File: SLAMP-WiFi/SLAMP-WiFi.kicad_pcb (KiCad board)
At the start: 2 copper layers, 61.6 x 47.2 mm, 50 parts, among them P1 POWER_IN 5V, P10 FACE5, P2 USB_BUS, P3 VUSB, P4 EXTRA, P5 ADC, P6 FACE1, P7 FACE2, P8 FACE3, P9 FACE4, Q1 S8050, Q2 S8050, SW1 KEY_RST, SW2 KEY_FLASH, U1 MIC5219-3.3BM5, U2 CH340G, U3 ESP-12F, Y1 12 MHz

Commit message: Serigrafia terminada
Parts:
- removed G***: LOGO, mod:wifilogo
- renumbered P5 to ADC, P4 to EXTRA, P6 to FACE1, P7 to FACE2, P8 to FACE3, P10 to FACE4, P9 to FACE5, SW2 to FLASH, SW1 to RESET
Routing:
- net (no net): track 0.00 -> 0.13 mm, vias 0 -> 8
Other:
- board text added: "GND"
- board text added: "Vin"
- board text added: "vUSB"

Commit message: Reparado error en el simbolo del transsitor S8050
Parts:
- added G***: LOGO, logos_frizzy:logo_wifi, F.Cu at (174.4, 85.5)
- added REF**: MountingHole_3.2mm_M3, Mounting_Holes:MountingHole_3.2mm_M3, F.Cu at (198.9, 85.9)
- added REF**: MountingHole_3.2mm_M3, Mounting_Holes:MountingHole_3.2mm_M3, F.Cu at (163.8, 65.8)
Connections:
- Q1 pad 1: RTS -> Net-(Q1-Pad1)
- Q1 pad 2: Net-(Q1-Pad2) -> RTS
- Q2 pad 1: DTR -> Net-(Q2-Pad1)
- Q2 pad 2: Net-(Q2-Pad2) -> DTR
- R17 pad 2: Net-(Q1-Pad2) -> Net-(Q1-Pad1)
- R18 pad 2: Net-(Q2-Pad2) -> Net-(Q2-Pad1)
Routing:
- net Net-(Q1-Pad1): track 0.00 -> 11.5 mm, vias 0 -> 2
- net Net-(Q2-Pad2): track 10.6 -> 0.00 mm, vias 2 -> 0
- net Net-(Q2-Pad1): track 0.00 -> 5.36 mm
- net Net-(Q1-Pad2): track 5.04 -> 0.00 mm
- net DTR: track 10.2 -> 14.1 mm
- net RTS: track 11.4 -> 8.37 mm
- net (no net): vias 8 -> 7

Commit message: Serigrafia añadida y taladros cambiados
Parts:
- added G***: LOGO, logos_frizzy:logo_slamp_wifi_oro, B.Cu at (198.5, 85.0)
- added G***: LOGO, logos_frizzy:wifi_ola, B.Cu at (198.5, 85.0)
- added G***: LOGO, logos_frizzy:web, F.Cu at (202.8, 89.0)
- G***: moved to B.Cu
- moved G*** 31.1 mm to (198.5, 65.9), turned to 180 degrees
- moved REF** 24.3 mm to (174.6, 84.8)
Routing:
- net (no net): vias 7 -> 6

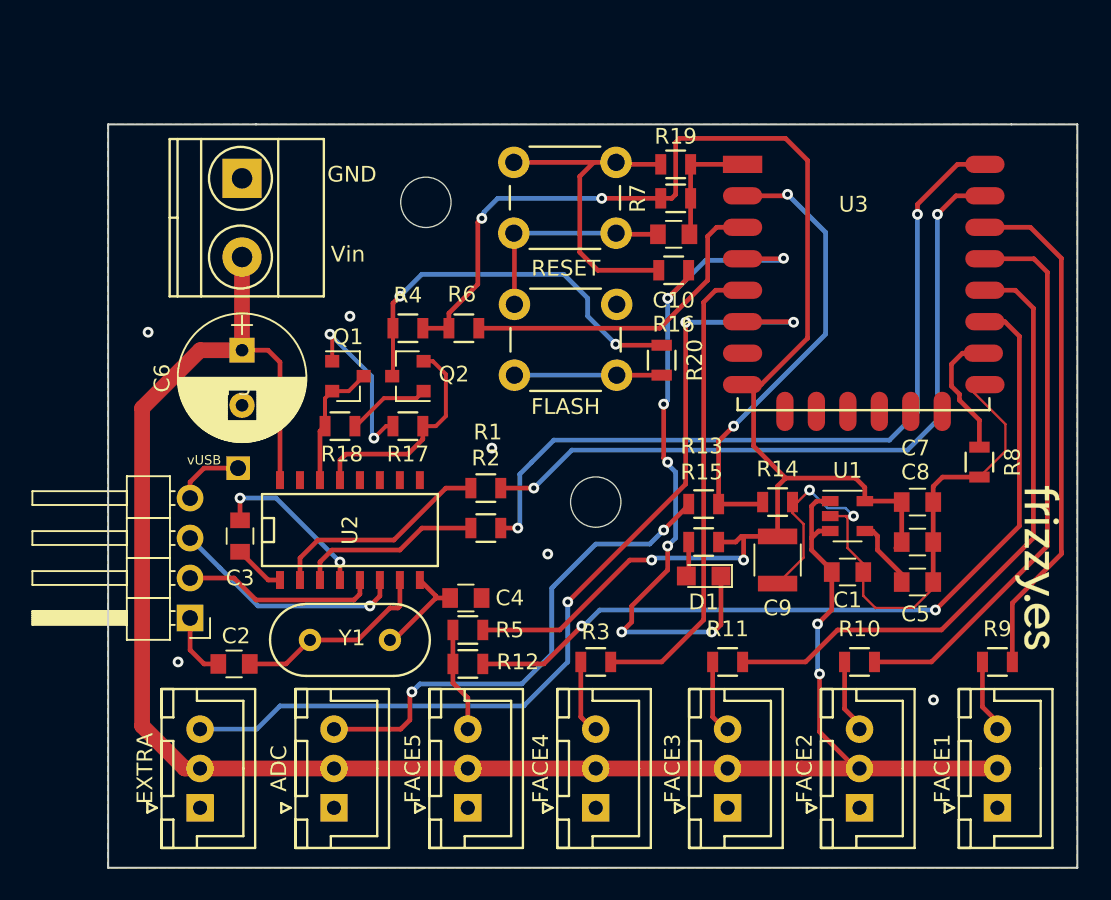
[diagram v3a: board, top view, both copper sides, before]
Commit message: Error con el GPIO0 arreglado
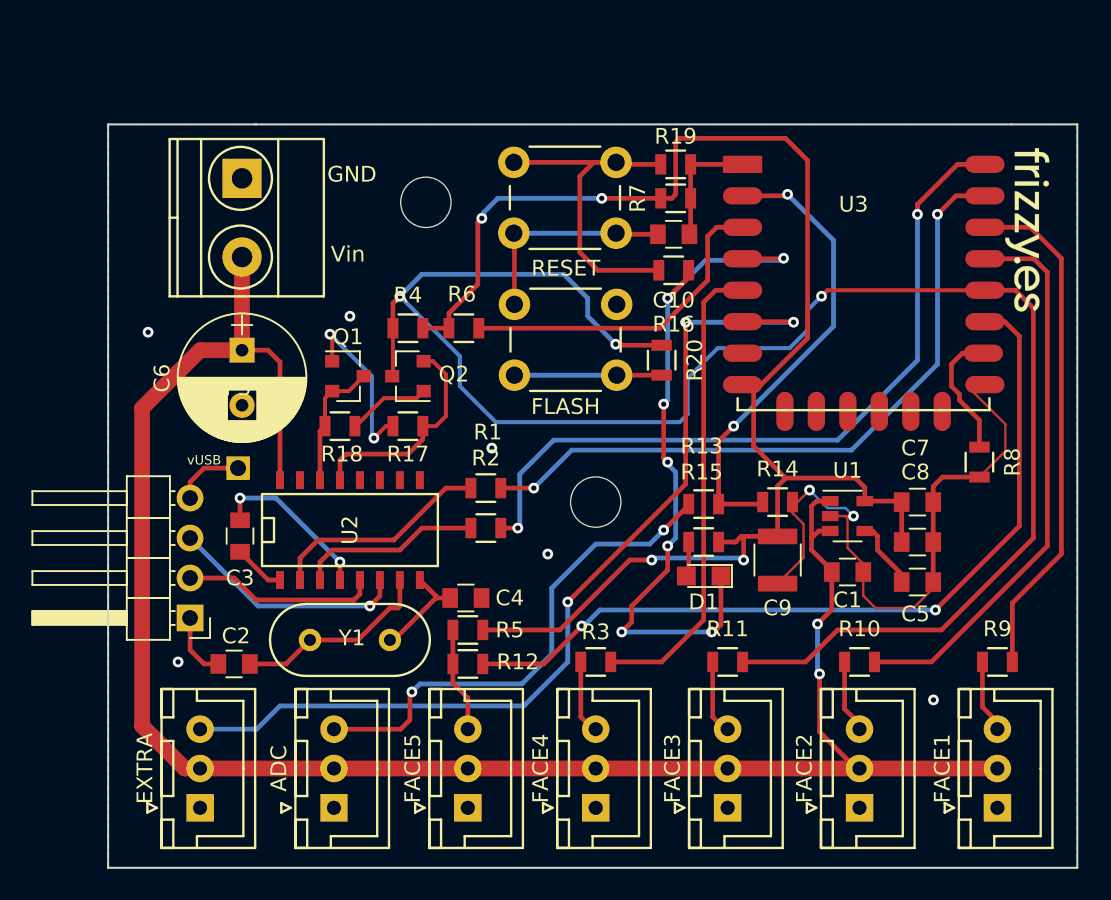
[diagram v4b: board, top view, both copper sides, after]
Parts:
- moved G*** 21.5 mm to (202.2, 67.6)
- moved G*** 0.74 mm to (198.1, 84.3) (x2)
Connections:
- R11 pad 2: Net-(R11-Pad2) -> GPIO0
- U3 pad 12: Net-(R11-Pad2) -> GPIO0
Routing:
- net GPIO0: track 25.1 -> 112.2 mm, vias 2 -> 3
- net Net-(R11-Pad2): track 40.6 -> 0.00 mm
- net TXD: track 45.4 -> 43.3 mm
- net RXD: track 49.4 -> 47.5 mm

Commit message: Problema con los RTS solucionado
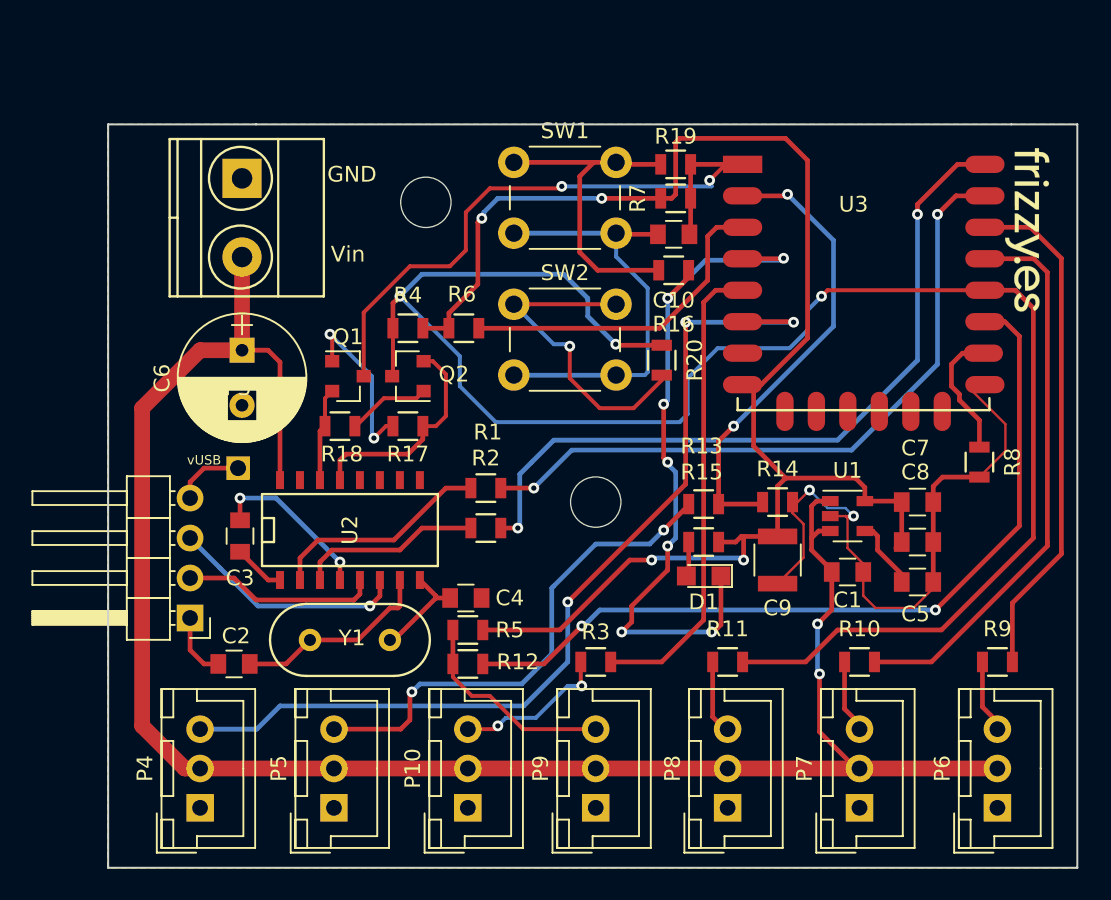
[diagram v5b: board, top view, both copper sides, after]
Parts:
- removed ADC: ADC, Connectors_JST:JST_XH_B03B-XH-A_03x2.50mm_Straight
- removed EXTRA: EXTRA, Connectors_JST:JST_XH_B03B-XH-A_03x2.50mm_Straight
- removed FACE1: FACE1, Connectors_JST:JST_XH_B03B-XH-A_03x2.50mm_Straight
- removed FACE2: FACE2, Connectors_JST:JST_XH_B03B-XH-A_03x2.50mm_Straight
- removed FACE3: FACE3, Connectors_JST:JST_XH_B03B-XH-A_03x2.50mm_Straight
- removed FACE4: FACE5, Connectors_JST:JST_XH_B03B-XH-A_03x2.50mm_Straight
- removed FACE5: FACE4, Connectors_JST:JST_XH_B03B-XH-A_03x2.50mm_Straight
- removed FLASH: KEY_FLASH, Buttons_Switches_THT:SW_PUSH_6mm
- removed RESET: KEY_RST, Buttons_Switches_THT:SW_PUSH_6mm
- added P10: FACE5, Connectors_JST:JST_XH_B03B-XH-A_03x2.50mm_Straight, F.Cu at (166.5, 104.3)
- added P4: EXTRA, Connectors_JST:JST_XH_B03B-XH-A_03x2.50mm_Straight, F.Cu at (149.5, 104.3)
- added P5: ADC, Connectors_JST:JST_XH_B03B-XH-A_03x2.50mm_Straight, F.Cu at (158.0, 104.3)
- added P6: FACE1, Connectors_JST:JST_XH_B03B-XH-A_03x2.50mm_Straight, F.Cu at (200.2, 104.3)
- added P7: FACE2, Connectors_JST:JST_XH_B03B-XH-A_03x2.50mm_Straight, F.Cu at (191.4, 104.3)
- added P8: FACE3, Connectors_JST:JST_XH_B03B-XH-A_03x2.50mm_Straight, F.Cu at (183.0, 104.3)
- added P9: FACE4, Connectors_JST:JST_XH_B03B-XH-A_03x2.50mm_Straight, F.Cu at (174.6, 104.3)
- added SW1: KEY_RST, Buttons_Switches_THT:SW_PUSH_6mm, F.Cu at (169.4, 63.2)
- added SW2: KEY_FLASH, Buttons_Switches_THT:SW_PUSH_6mm, F.Cu at (169.4, 72.3)
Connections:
- C10 pad 1: RST -> uRST
- Q1 pad 3: RTS -> uRST
- R19 pad 1: RST -> uRST
- R7 pad 1: RST -> uRST
- U3 pad 1: RST -> uRST
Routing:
- net uRST: track 0.00 -> 43.0 mm, vias 0 -> 2
- net GND: track 61.6 -> 75.4 mm
- net Net-(R20-Pad2): track 9.36 -> 20.9 mm, vias 0 -> 1
- net RST: track 8.48 -> 0.00 mm
- net FACE4: track 7.28 -> 13.6 mm
- net FACE5: track 4.77 -> 10.5 mm, vias 0 -> 2
- net RTS: track 8.37 -> 5.98 mm
- net (no net): track 0.13 -> 0.00 mm, vias 6 -> 0

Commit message: Sensores tactiles añadidos
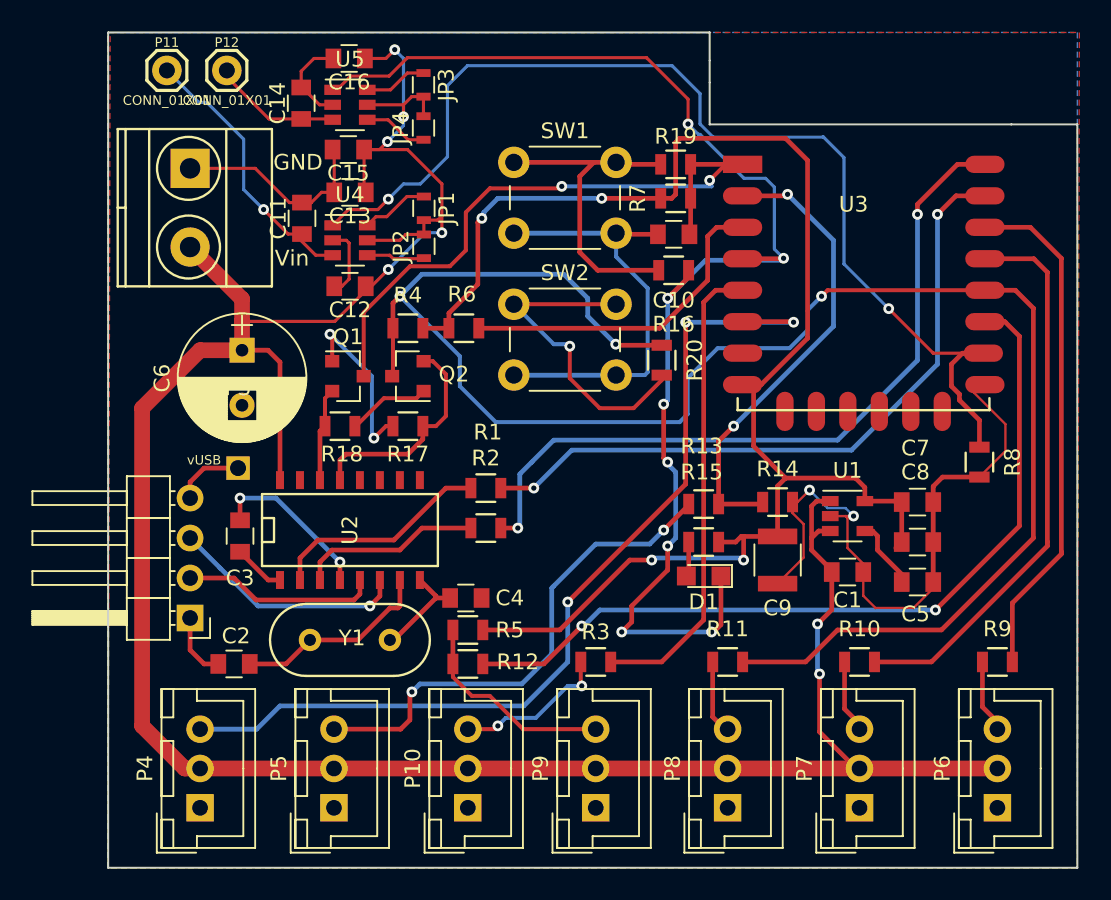
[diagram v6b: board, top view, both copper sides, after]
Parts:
- removed G***: LOGO, logos_frizzy:logo_wifi
- removed G***: LOGO, logos_frizzy:web
- removed G***: LOGO, logos_frizzy:wifi_ola
- removed G***: LOGO, logos_frizzy:logo_slamp_wifi_oro
- removed REF** (x2): MountingHole_3.2mm_M3, Mounting_Holes:MountingHole_3.2mm_M3
- added C11: 30p, Capacitors_SMD:C_0805, F.Cu at (156.0, 66.8)
- added C12: 100n, Capacitors_SMD:C_0805, F.Cu at (159.0, 71.1)
- added C13: 10uF, Capacitors_SMD:C_0805, F.Cu at (159.0, 65.2)
- added C14: 30p, Capacitors_SMD:C_0805, F.Cu at (155.9, 59.5)
- added C15: 100n, Capacitors_SMD:C_0805, F.Cu at (158.9, 62.4)
- added C16: 10uF, Capacitors_SMD:C_0805, F.Cu at (159.0, 56.6)
- added JP1: Jumper, Resistors_SMD:R_0603, F.Cu at (163.7, 66.2)
- added JP2: Jumper, Resistors_SMD:R_0603, F.Cu at (163.7, 68.6)
- added JP3: Jumper, Resistors_SMD:R_0603, F.Cu at (163.7, 58.3)
- added JP4: Jumper, Resistors_SMD:R_0603, F.Cu at (163.7, 61.1)
- added P11: CONN_01X01, Connectors:1X01, F.Cu at (147.4, 57.4)
- added P12: CONN_01X01, Connectors:1X01, F.Cu at (151.2, 57.4)
- added U4: TTP223, TO_SOT_Packages_SMD:SOT-23-6, F.Cu at (159.0, 68.2)
- added U5: TTP223, TO_SOT_Packages_SMD:SOT-23-6, F.Cu at (159.0, 59.6)
- moved P1 3.36 mm to (148.8, 63.6)
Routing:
- net GPIO15: track 7.73 -> 68.0 mm, vias 0 -> 2
- net 5V: track 121.2 -> 172.2 mm, vias 2 -> 7
- net GPIO16: track 45.3 -> 83.3 mm, vias 7 -> 8
- net GND: track 75.4 -> 98.9 mm
- net Net-(C11-Pad1): track 0.00 -> 17.6 mm, vias 0 -> 1
- net Net-(C14-Pad1): track 0.00 -> 8.26 mm
- net Net-(JP1-Pad1): track 0.00 -> 4.36 mm
- net Net-(JP4-Pad1): track 0.00 -> 4.10 mm
- net Net-(JP3-Pad1): track 0.00 -> 4.02 mm
- net Net-(JP2-Pad1): track 0.00 -> 3.73 mm
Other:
- board size 61.6 x 47.2 mm -> 61.6 x 53.1 mm

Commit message: Serigrafia terminada
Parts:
- added G***: LOGO, Grape:web, F.Cu at (203.0, 71.1)
- added REF**: MountingHole_2.2mm_M2, Mounting_Holes:MountingHole_2.2mm_M2, F.Cu at (175.0, 84.3)
- added REF**: MountingHole_2.2mm_M2, Mounting_Holes:MountingHole_2.2mm_M2, F.Cu at (175.1, 59.1)
- P11: value CONN_01X01 -> GPIO15
- P12: value CONN_01X01 -> GPIO16
- renumbered P5 to ANALOG, U3 to ESP12E, P4 to EXTRA, P6 to FACE1, P7 to FACE2, P8 to FACE3, P9 to FACE4, P10 to FACE5, SW2 to FLASH, SW1 to RESET
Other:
- board text added: "D+"
- board text added: "D-"
- board text added: "Vusb"

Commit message: mandada a fabrica
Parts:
- added G***: LOGO, logos_frizzy:logo_slamp_wifi_oro, B.Cu at (198.8, 85.3)
- added G***: LOGO, logos_frizzy:wifi_ola, B.Cu at (198.7, 85.3)
- added G***: LOGO, logos_frizzy:logo_wifi, B.Cu at (198.7, 65.8)
- added REF**: MountingHole_2.2mm_M2, Mounting_Holes:MountingHole_2.2mm_M2, F.Cu at (146.6, 74.0)
- added REF***: OSHW-Symbol_6.7x6mm_SilkScreen, Symbols:OSHW-Symbol_6.7x6mm_SilkScreen, B.Cu at (198.9, 74.2)
- moved REF** 2.65 mm to (172.5, 85.1)
- moved REF** 2.60 mm to (172.5, 58.9)
